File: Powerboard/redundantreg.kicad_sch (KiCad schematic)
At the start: 28 parts, among them Q10 MCH6351, Q9 MCH6351, U6 LM2679T-3.3-iclr, U7 LM2679T-3.3-iclr, U8 LTC4412xS6, U9 LTC4412xS6

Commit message: update
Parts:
- removed TP19, TP20, TP21, TP22: TestPoint, TestPoint:TestPoint_Pad_D1.0mm, symbol Connector:TestPoint
- C43: value 0.47uF -> 0.47μF
- C48, C49: value 0.1uF -> 0.1µF
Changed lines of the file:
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@@
   (junction (at 190.5 44.45) (diameter 0) (color 0 0 0 0)
   )
-  (junction (at 234.95 34.29) (diameter 0) (color 0 0 0 0)
-  )
   (junction (at 163.83 163.83) (diameter 0) (color 0 0 0 0)
   )
@@
   (junction (at 133.35 41.91) (diameter 0) (color 0 0 0 0)
   )
-  (junction (at 74.93 25.4) (diameter 0) (color 0 0 0 0)
-  )
-  (junction (at 240.03 147.32) (diameter 0) (color 0 0 0 0)
-  )
   (junction (at 163.83 147.32) (diameter 0) (color 0 0 0 0)
   )
@@
   )
   (junction (at 68.58 25.4) (diameter 0) (color 0 0 0 0)
-  )
-  (junction (at 78.74 147.32) (diameter 0) (color 0 0 0 0)
   )
   (junction (at 190.5 25.4) (diameter 0) (color 0 0 0 0)
@@
     (stroke (width 0) (type default) (color 0 0 0 0))
   )
-  (wire (pts (xy 228.6 34.29) (xy 234.95 34.29))
+  (wire (pts (xy 228.6 34.29) (xy 257.81 34.29))
     (stroke (width 0) (type default) (color 0 0 0 0))
   )
@@
     (stroke (width 0) (type default) (color 0 0 0 0))
   )
-  (wire (pts (xy 234.95 34.29) (xy 257.81 34.29))
-    (stroke (width 0) (type default) (color 0 0 0 0))
-  )
   (wire (pts (xy 158.75 41.91) (xy 163.83 41.91))
     (stroke (width 0) (type default) (color 0 0 0 0))
@@
     (stroke (width 0) (type default) (color 0 0 0 0))
   )
-  (wire (pts (xy 74.93 25.4) (xy 80.01 25.4))
-    (stroke (width 0) (type default) (color 0 0 0 0))
-  )
   (wire (pts (xy 222.25 34.29) (xy 228.6 34.29))
     (stroke (width 0) (type default) (color 0 0 0 0))
@@
     (stroke (width 0) (type default) (color 0 0 0 0))
   )
-  (wire (pts (xy 240.03 147.32) (xy 257.81 147.32))
+  (wire (pts (xy 233.68 147.32) (xy 257.81 147.32))
     (stroke (width 0) (type default) (color 0 0 0 0))
   )
@@
     (stroke (width 0) (type default) (color 0 0 0 0))
   )
-  (wire (pts (xy 233.68 147.32) (xy 240.03 147.32))
-    (stroke (width 0) (type default) (color 0 0 0 0))
-  )
   (wire (pts (xy 171.45 130.81) (xy 189.23 130.81))
     (stroke (width 0) (type default) (color 0 0 0 0))
@@
     (stroke (width 0) (type default) (color 0 0 0 0))
   )
-  (wire (pts (xy 69.85 147.32) (xy 78.74 147.32))
+  (wire (pts (xy 69.85 147.32) (xy 81.28 147.32))
     (stroke (width 0) (type default) (color 0 0 0 0))
   )
@@
     (stroke (width 0) (type default) (color 0 0 0 0))
   )
-  (wire (pts (xy 78.74 147.32) (xy 81.28 147.32))
-    (stroke (width 0) (type default) (color 0 0 0 0))
-  )
   (wire (pts (xy 64.77 34.29) (xy 64.77 41.91))
     (stroke (width 0) (type default) (color 0 0 0 0))
@@
     (stroke (width 0) (type default) (color 0 0 0 0))
   )
-  (wire (pts (xy 68.58 25.4) (xy 74.93 25.4))
+  (wire (pts (xy 68.58 25.4) (xy 80.01 25.4))
     (stroke (width 0) (type default) (color 0 0 0 0))
   )
@@
       (effects (font (size 1.27 1.27)) (justify left))
     )
-    (property "Value" "0.47uF" (id 1) (at 72.1868 157.353 0)
+    (property "Value" "0.47μF" (id 1) (at 72.1868 157.353 0)
       (effects (font (size 1.27 1.27)) (justify left))
     )
@@
     (in_bom yes) (on_board yes)
     (property "Reference" "C48" (id 0) (at 168.91 125.095 90))
-    (property "Value" "0.1uF" (id 1) (at 168.91 127.4064 90))
+    (property "Value" "0.1µF" (id 1) (at 168.91 127.4064 90))
     (property "Footprint" "Capacitor_SMD:C_0603_1608Metric" (id 2) (at 168.91 130.81 0)
       (effects (font (size 1.27 1.27)) hide)
@@
     (in_bom yes) (on_board yes)
     (property "Reference" "C49" (id 0) (at 186.69 38.735 90))
-    (property "Value" "0.1uF" (id 1) (at 186.69 41.0464 90))
+    (property "Value" "0.1µF" (id 1) (at 186.69 41.0464 90))
     (property "Footprint" "Capacitor_SMD:C_0603_1608Metric" (id 2) (at 186.69 44.45 0)
       (effects (font (size 1.27 1.27)) hide)
@@
     (pin "2")
   )
-  (symbol (lib_id "Connector:TestPoint") (at 234.95 34.29 0) (unit 1)
-    (in_bom yes) (on_board yes)
-    (property "Reference" "TP21" (id 0) (at 236.4232 31.2928 0)
-      (effects (font (size 1.27 1.27)) (justify left))
-    )
-    (property "Value" "TestPoint" (id 1) (at 236.4232 33.6042 0)
-      (effects (font (size 1.27 1.27)) (justify left))
-    )
-    (property "Footprint" "TestPoint:TestPoint_Pad_D1.0mm" (id 2) (at 240.03 34.29 0)
-      (effects (font (size 1.27 1.27)) hide)
-    )
-    (property "Datasheet" "~" (id 3) (at 240.03 34.29 0)
-      (effects (font (size 1.27 1.27)) hide)
-    )
-    (pin "1")
-  )
-  (symbol (lib_id "Connector:TestPoint") (at 240.03 147.32 180) (unit 1)
-    (in_bom yes) (on_board yes)
-    (property "Reference" "TP22" (id 0) (at 241.5032 147.9804 0)
-      (effects (font (size 1.27 1.27)) (justify right))
-    )
-    (property "Value" "TestPoint" (id 1) (at 241.5032 150.2918 0)
-      (effects (font (size 1.27 1.27)) (justify right))
-    )
-    (property "Footprint" "TestPoint:TestPoint_Pad_D1.0mm" (id 2) (at 234.95 147.32 0)
-      (effects (font (size 1.27 1.27)) hide)
-    )
-    (property "Datasheet" "~" (id 3) (at 234.95 147.32 0)
-      (effects (font (size 1.27 1.27)) hide)
-    )
-    (pin "1")
-  )
-  (symbol (lib_id "Connector:TestPoint") (at 74.93 25.4 0) (unit 1)
-    (in_bom yes) (on_board yes)
-    (property "Reference" "TP19" (id 0) (at 76.4032 22.4028 0)
-      (effects (font (size 1.27 1.27)) (justify left))
-    )
-    (property "Value" "TestPoint" (id 1) (at 76.4032 24.7142 0)
-      (effects (font (size 1.27 1.27)) (justify left))
-    )
-    (property "Footprint" "TestPoint:TestPoint_Pad_D1.0mm" (id 2) (at 80.01 25.4 0)
-      (effects (font (size 1.27 1.27)) hide)
-    )
-    (property "Datasheet" "~" (id 3) (at 80.01 25.4 0)
-      (effects (font (size 1.27 1.27)) hide)
-    )
-    (pin "1")
-  )
-  (symbol (lib_id "Connector:TestPoint") (at 78.74 147.32 0) (unit 1)
-    (in_bom yes) (on_board yes)
-    (property "Reference" "TP20" (id 0) (at 80.2132 144.3228 0)
-      (effects (font (size 1.27 1.27)) (justify left))
-    )
-    (property "Value" "TestPoint" (id 1) (at 80.2132 146.6342 0)
-      (effects (font (size 1.27 1.27)) (justify left))
-    )
-    (property "Footprint" "TestPoint:TestPoint_Pad_D1.0mm" (id 2) (at 83.82 147.32 0)
-      (effects (font (size 1.27 1.27)) hide)
-    )
-    (property "Datasheet" "~" (id 3) (at 83.82 147.32 0)
-      (effects (font (size 1.27 1.27)) hide)
-    )
-    (pin "1")
-  )
   (symbol (lib_id "iclr:LM2679T-3.3-iclr") (at 102.87 25.4 0) (unit 1)

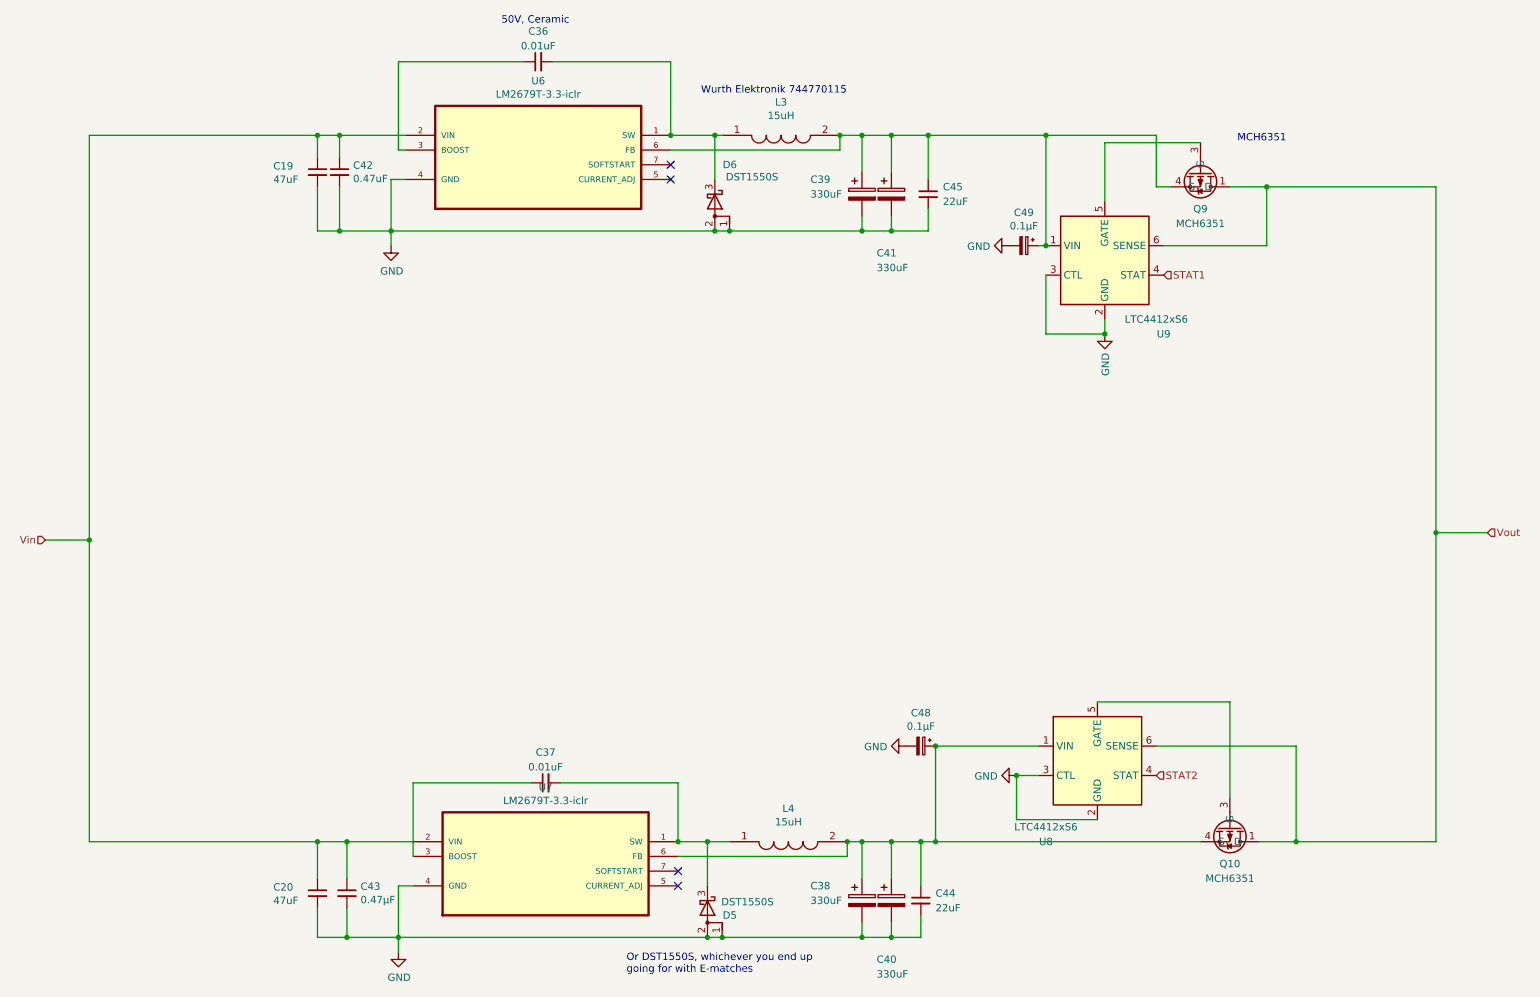
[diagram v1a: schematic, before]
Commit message: Changed some values and footprints since some went out of stock
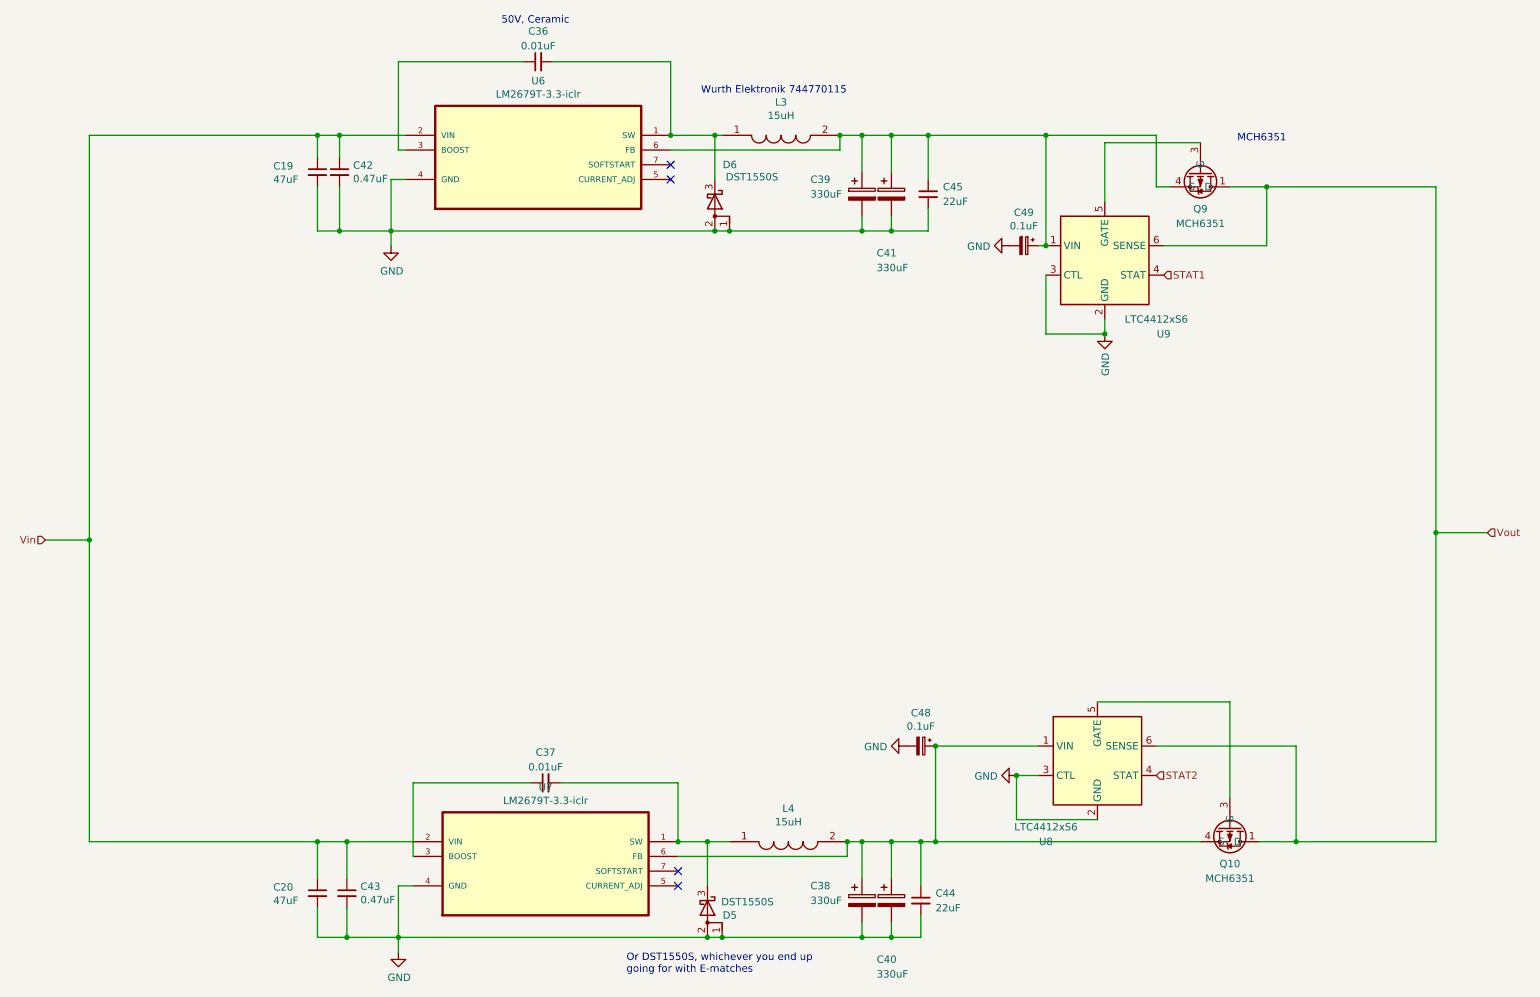
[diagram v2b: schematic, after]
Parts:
- C43: value 0.47μF -> 0.47uF
- C48, C49: value 0.1µF -> 0.1uF
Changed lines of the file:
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@@
       (effects (font (size 1.27 1.27)) (justify left))
     )
-    (property "Value" "0.47μF" (id 1) (at 72.1868 157.353 0)
+    (property "Value" "0.47uF" (id 1) (at 72.1868 157.353 0)
       (effects (font (size 1.27 1.27)) (justify left))
     )
@@
     (in_bom yes) (on_board yes)
     (property "Reference" "C48" (id 0) (at 168.91 125.095 90))
-    (property "Value" "0.1µF" (id 1) (at 168.91 127.4064 90))
+    (property "Value" "0.1uF" (id 1) (at 168.91 127.4064 90))
     (property "Footprint" "Capacitor_SMD:C_0603_1608Metric" (id 2) (at 168.91 130.81 0)
       (effects (font (size 1.27 1.27)) hide)
@@
     (in_bom yes) (on_board yes)
     (property "Reference" "C49" (id 0) (at 186.69 38.735 90))
-    (property "Value" "0.1µF" (id 1) (at 186.69 41.0464 90))
+    (property "Value" "0.1uF" (id 1) (at 186.69 41.0464 90))
     (property "Footprint" "Capacitor_SMD:C_0603_1608Metric" (id 2) (at 186.69 44.45 0)
       (effects (font (size 1.27 1.27)) hide)
